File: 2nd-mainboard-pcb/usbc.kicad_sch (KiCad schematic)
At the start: 11 parts, among them P1 USB_C_Receptacle_USB2.0_14P, U5 FT232RL, U6 PTS647SM38SMTR2LFS

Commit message: rearragned componentens
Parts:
- C16, C17: footprint Capacitor_SMD:C_0402_1005Metric_Pad0.74x0.62mm_HandSolder -> Capacitor_SMD:C_0603_1608Metric_Pad1.08x0.95mm_HandSolder
- R10, R11, R9: footprint Resistor_SMD:R_0402_1005Metric -> Resistor_SMD:R_0603_1608Metric_Pad0.98x0.95mm_HandSolder
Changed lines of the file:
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@@
 			)
 		)
-		(property "Footprint" "Capacitor_SMD:C_0402_1005Metric_Pad0.74x0.62mm_HandSolder"
+		(property "Footprint" "Capacitor_SMD:C_0603_1608Metric_Pad1.08x0.95mm_HandSolder"
 			(at 207.9752 43.18 0)
 			(effects
@@
 			)
 		)
-		(property "Footprint" "Resistor_SMD:R_0402_1005Metric"
+		(property "Footprint" "Resistor_SMD:R_0603_1608Metric_Pad0.98x0.95mm_HandSolder"
 			(at 66.802 59.69 90)
 			(effects
@@
 			)
 		)
-		(property "Footprint" "Resistor_SMD:R_0402_1005Metric"
+		(property "Footprint" "Resistor_SMD:R_0603_1608Metric_Pad0.98x0.95mm_HandSolder"
 			(at 94.742 138.43 90)
 			(effects
@@
 			)
 		)
-		(property "Footprint" "Resistor_SMD:R_0402_1005Metric"
+		(property "Footprint" "Resistor_SMD:R_0603_1608Metric_Pad0.98x0.95mm_HandSolder"
 			(at 75.692 59.69 90)
 			(effects
@@
 			)
 		)
-		(property "Footprint" "Capacitor_SMD:C_0402_1005Metric_Pad0.74x0.62mm_HandSolder"
+		(property "Footprint" "Capacitor_SMD:C_0603_1608Metric_Pad1.08x0.95mm_HandSolder"
 			(at 130.5052 40.64 0)
 			(effects

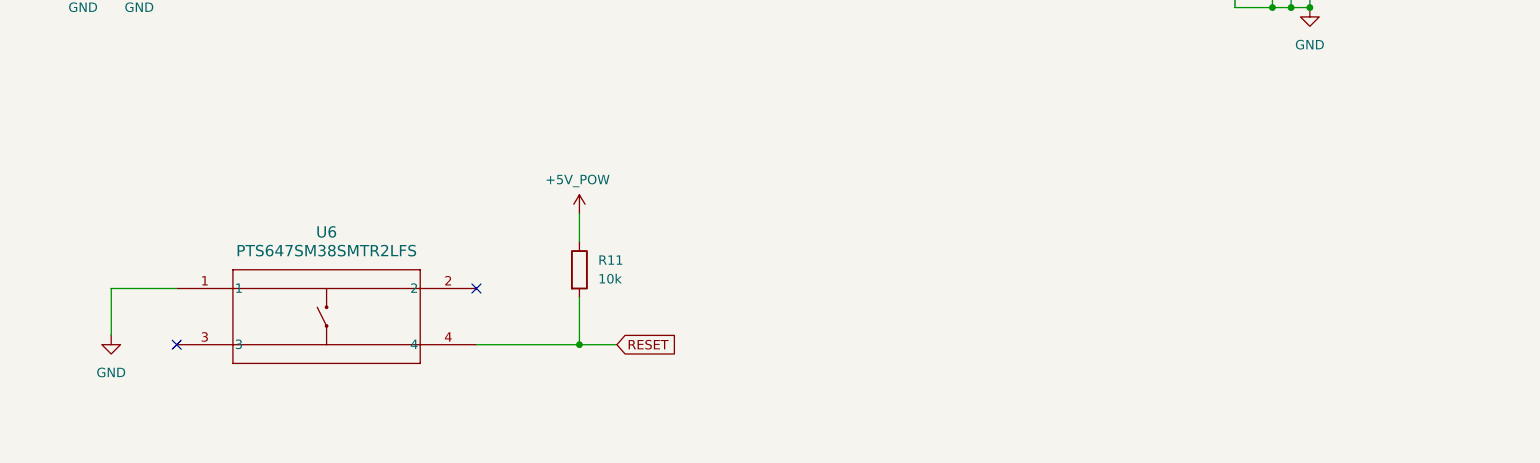
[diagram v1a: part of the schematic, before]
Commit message: layout optimiert, kondensatoren angepasst
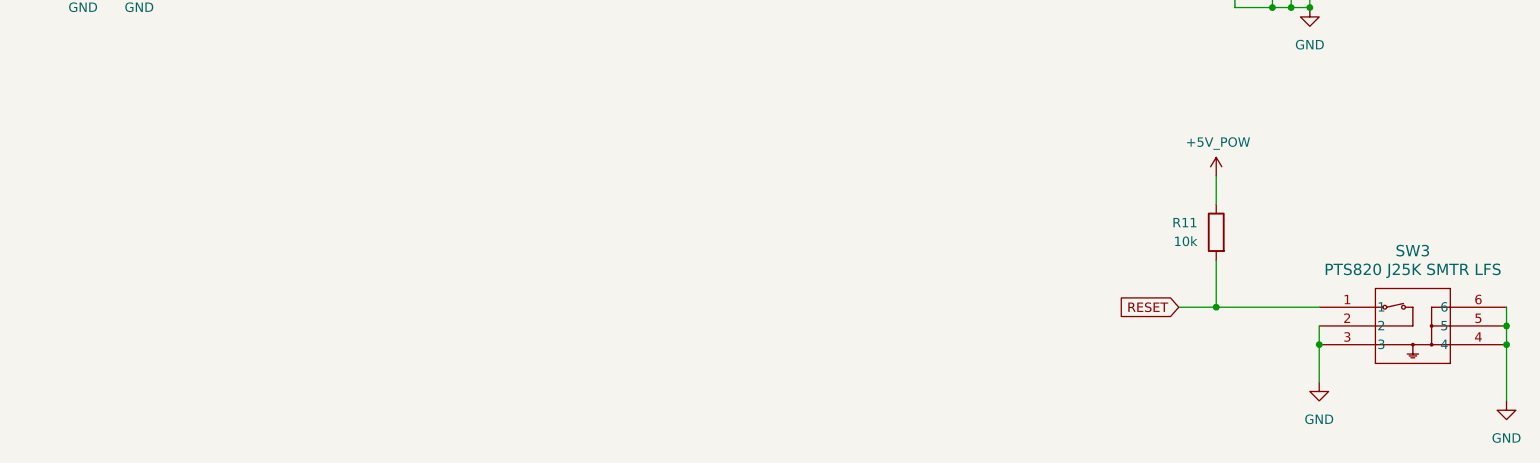
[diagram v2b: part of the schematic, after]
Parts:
- removed U6: PTS647SM38SMTR2LFS, Imported_Component_Footprints:SW_PTS647SM38SMTR2LFS_CNK, symbol Imported_Component_Symbols:PTS647SM38SMTR2LFS
- added SW3: PTS820 J25K SMTR LFS, Imported_Component_Footprints:PTS820 J25K SMTR LFS_CNK, symbol Imported_Component_Symbols:PTS820_J25K_SMTR_LFS
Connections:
- net GND: now also SW3.2, SW3.3, SW3.4, SW3.5, SW3.6
- net RESET: now also SW3.1
- no-connect marks 17 -> 15
